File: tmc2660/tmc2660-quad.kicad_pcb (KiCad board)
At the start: 4 copper layers, 124 x 40 mm, 74 parts, among them J1 Power, J100 0R, J2 DataIn, J200 0R, J300 0R, J400 0R, M100 Mount, M101 Mount, M200 Mount, M201 Mount, M300 Mount, M301 Mount, M400 Mount, M401 Mount, P100 Motor, P200 Motor, P300 Motor, P400 Motor, U100 TMC2660, U200 TMC2660, U300 TMC2660, U400 TMC2660

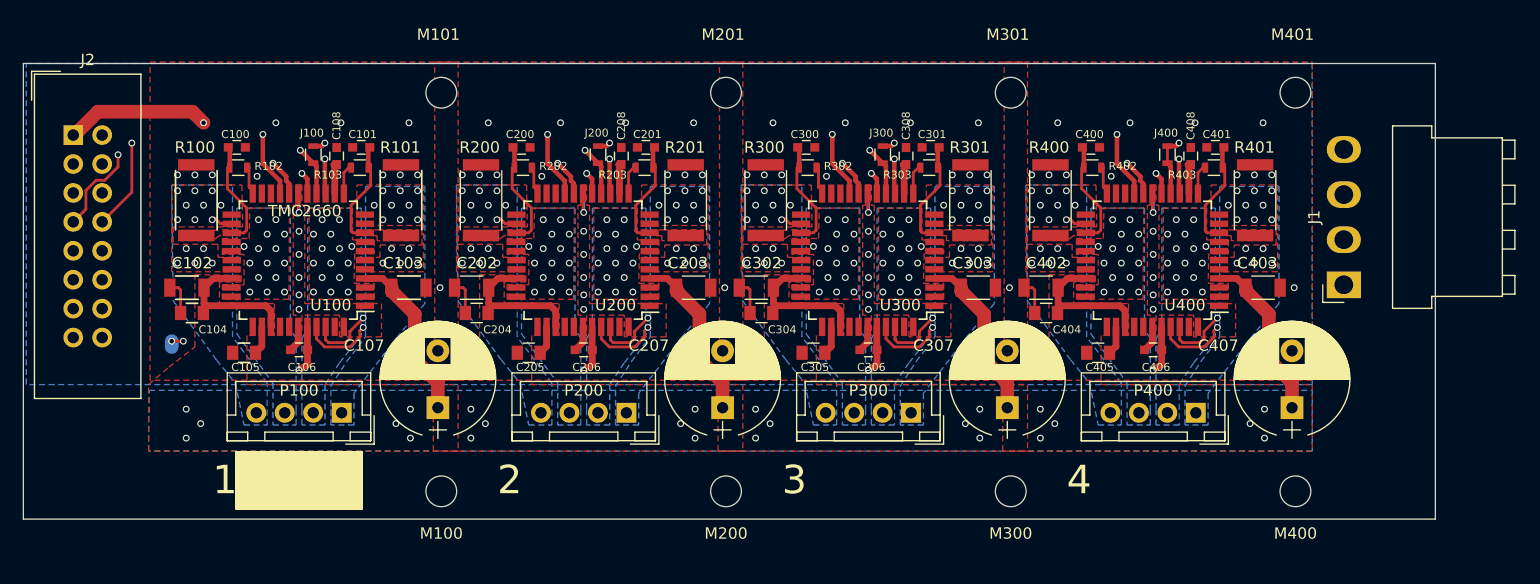
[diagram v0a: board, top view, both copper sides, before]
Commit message: Add leftmost screw holes; Move IDC connector down.
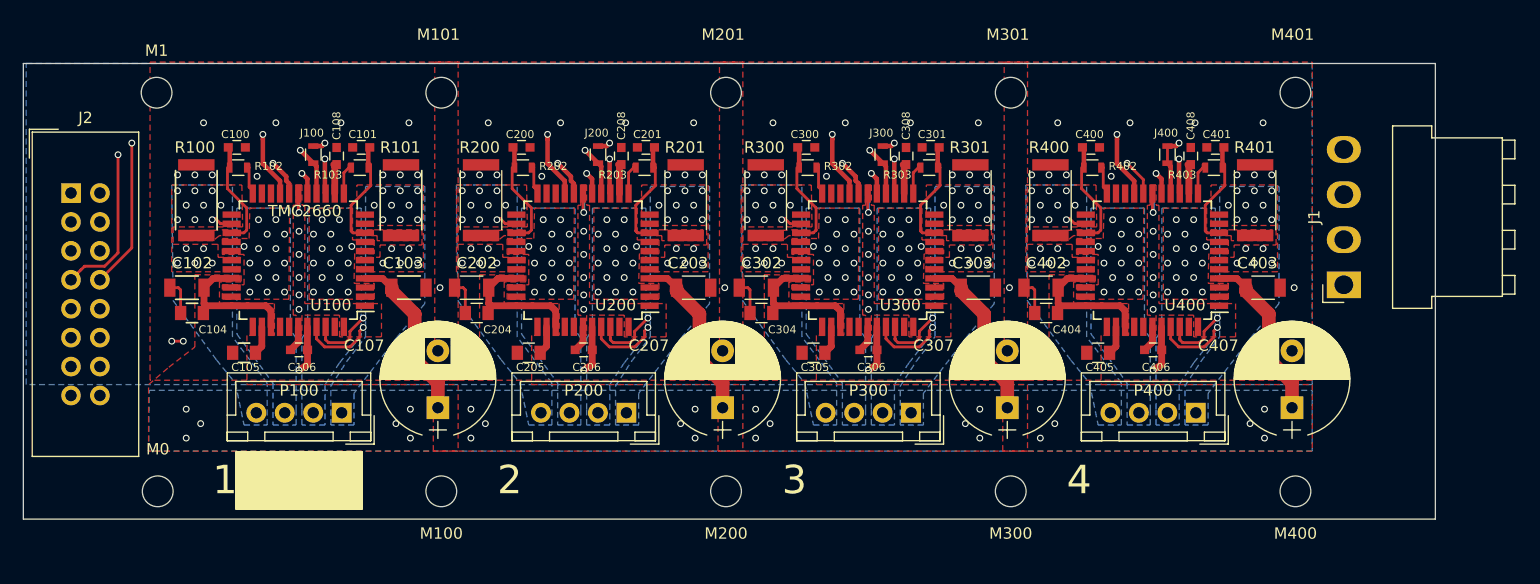
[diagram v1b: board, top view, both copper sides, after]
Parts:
- added M0: Mount, Mounting_Holes:MountingHole_2.7mm_M2.5, F.Cu at (71.4, 86.1)
- added M1: Mount, Mounting_Holes:MountingHole_2.7mm_M2.5, F.Cu at (71.3, 51.1)
- moved J2 5.09 mm to (63.8, 59.9)
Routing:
- net VCC: track 60.7 -> 38.4 mm
- net GND: track 52.5 -> 39.3 mm
- net GLOBAL_MISO: track 29.7 -> 35.4 mm
- net GLOBAL_MOSI: track 108.7 -> 113.9 mm
- net ~ENABLE: track 116.0 -> 120.1 mm
- net SCLK: track 103.1 -> 106.9 mm
- net STEP1: track 36.2 -> 32.7 mm
- net DIR4: track 108.9 -> 112.3 mm
- net CS: track 109.5 -> 112.8 mm
- net STEP4: track 110.8 -> 114.0 mm
- net DIR1: track 32.4 -> 30.7 mm
- net DIR3: track 83.6 -> 85.0 mm
- net STEP3: track 86.0 -> 87.0 mm
- net STEP2: track 60.8 -> 60.2 mm
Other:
- net class Default: clearance 0.127 -> 0.1524
- net class MotPower: clearance 0.127 -> 0.2032
- rule trace_clearance: 0.127 -> 0.1524

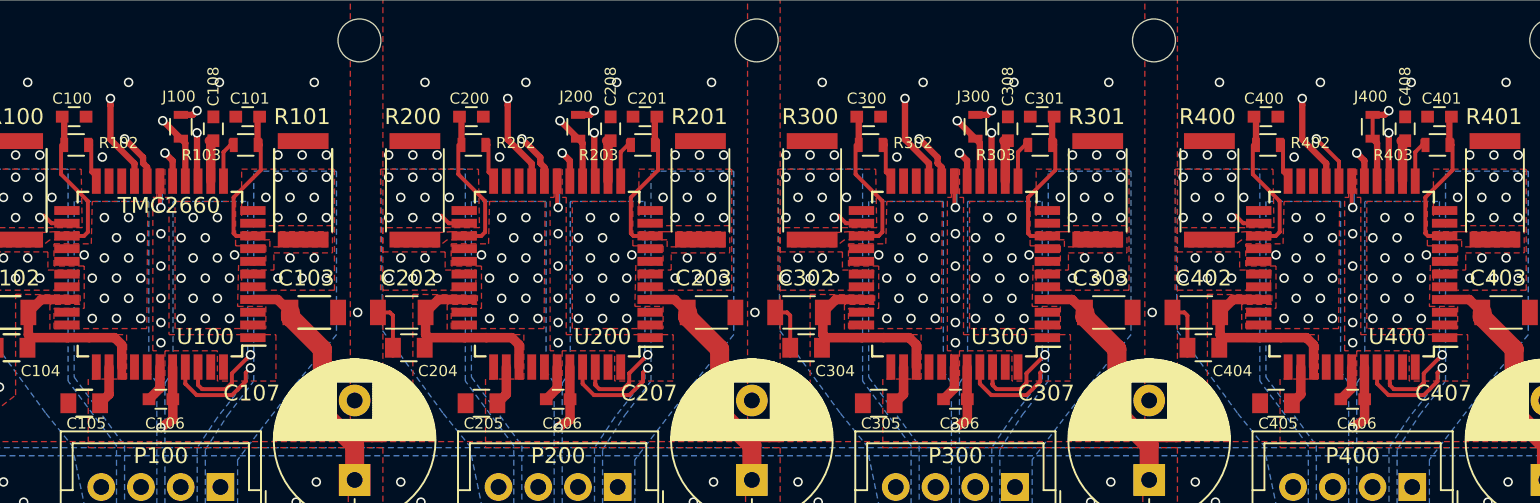
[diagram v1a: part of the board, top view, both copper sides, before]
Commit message: More conservative design rules in quad.
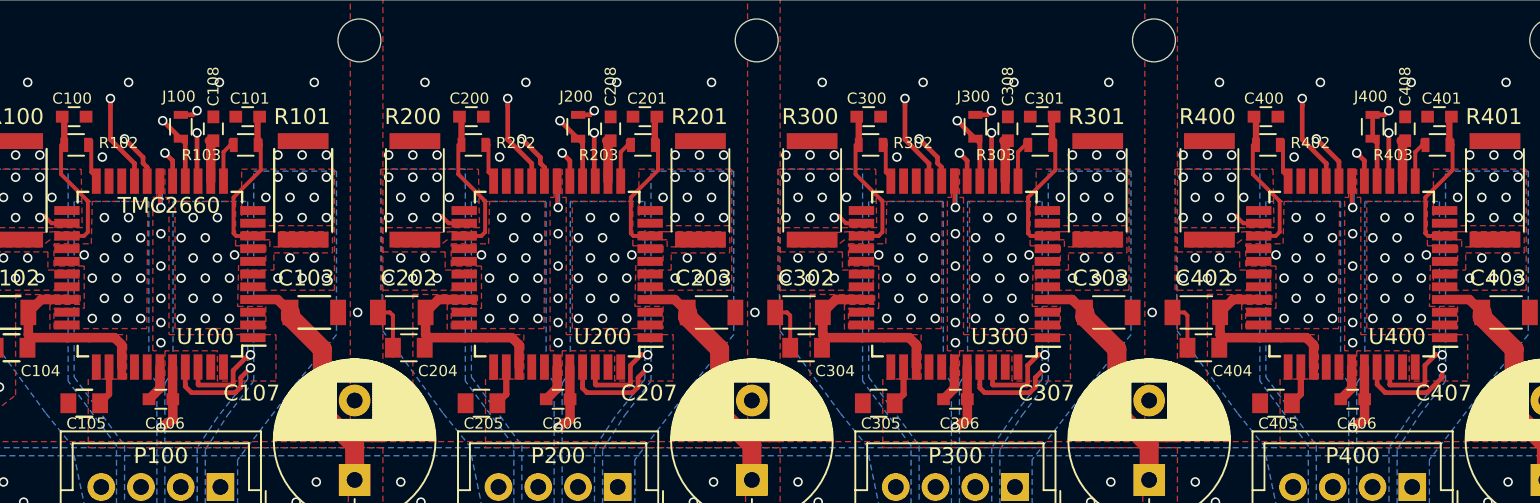
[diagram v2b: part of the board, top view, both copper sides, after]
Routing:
- net CS: track 112.8 -> 106.7 mm
- net GLOBAL_MISO: track 35.4 -> 32.1 mm
- net ~ENABLE: track 120.1 -> 117.0 mm
- net GLOBAL_MOSI: track 113.9 -> 111.4 mm
- net SCLK: track 106.9 -> 104.7 mm
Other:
- net class Default: clearance 0.1524 -> 0.18
- net class MotPower: clearance 0.2032 -> 0.21
- rule trace_clearance: 0.1524 -> 0.18

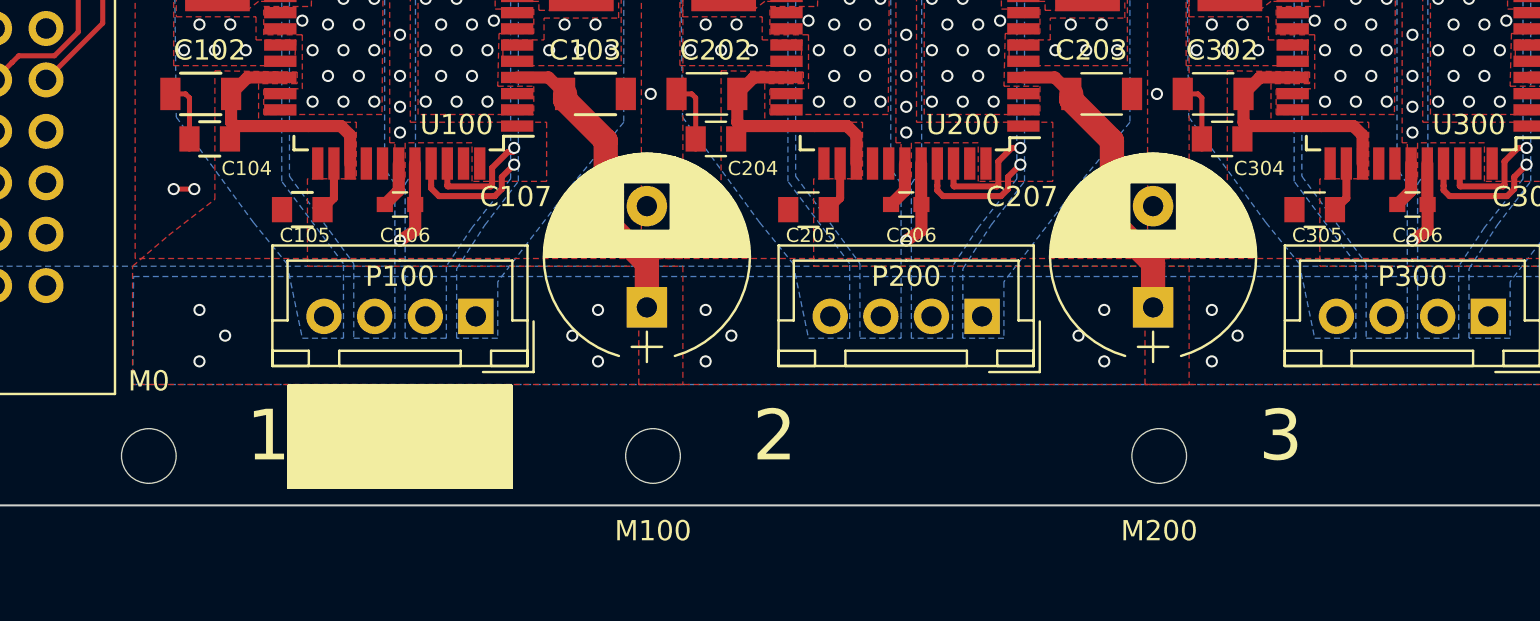
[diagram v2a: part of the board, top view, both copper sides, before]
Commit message: Routing of Step/Dir signals with new design rules.
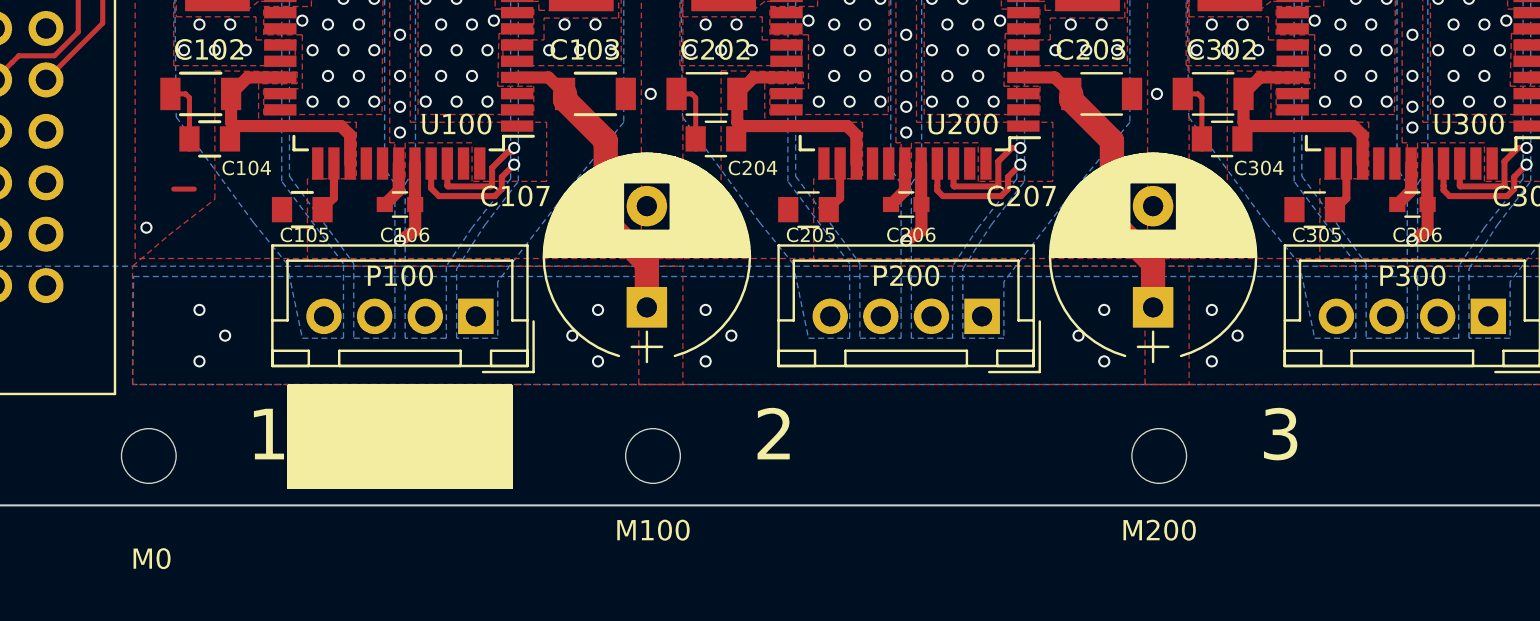
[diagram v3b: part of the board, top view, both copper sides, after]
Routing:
- net VCC: track 38.4 -> 54.1 mm
- net CS: track 106.7 -> 112.8 mm
- net GLOBAL_MISO: track 32.1 -> 35.4 mm
- net ~ENABLE: track 117.0 -> 120.1 mm
- net GLOBAL_MOSI: track 111.4 -> 113.9 mm
- net SCLK: track 104.7 -> 106.7 mm
- net DIR4: track 112.2 -> 111.5 mm
- net STEP4: track 114.1 -> 113.3 mm
- net STEP2: track 60.3 -> 60.8 mm
- net GND: vias 92 -> 91

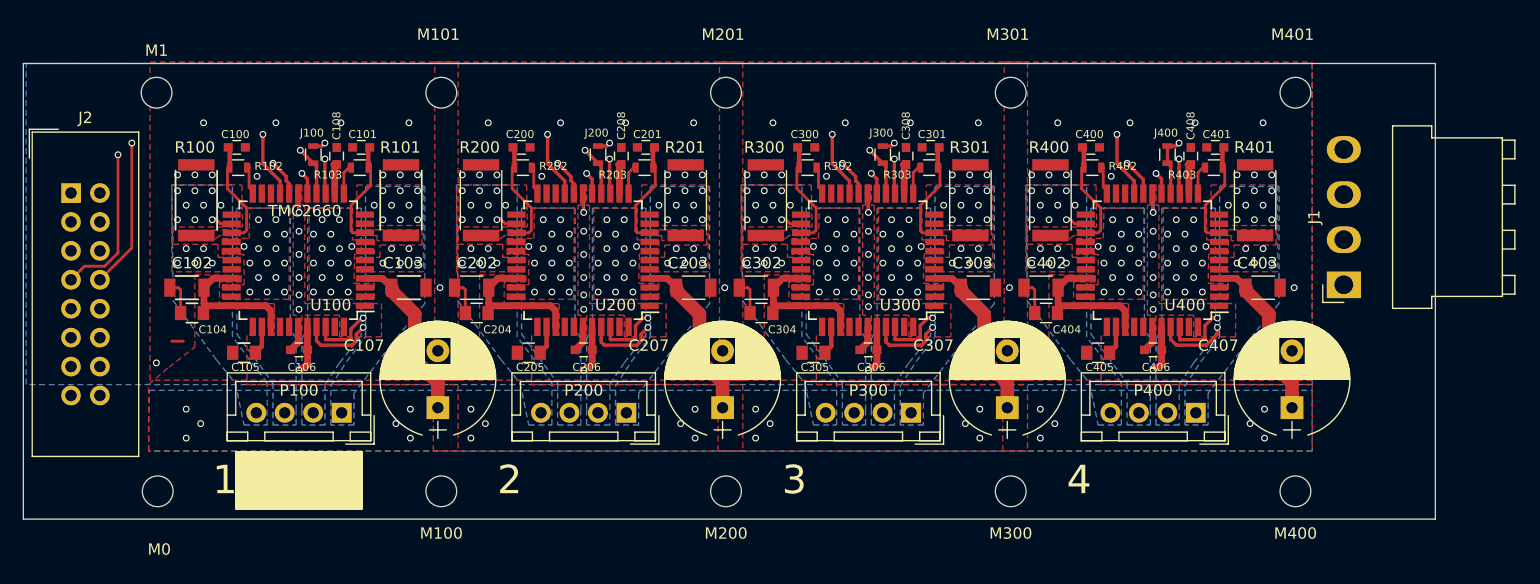
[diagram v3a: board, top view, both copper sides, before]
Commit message: Add a fuse.
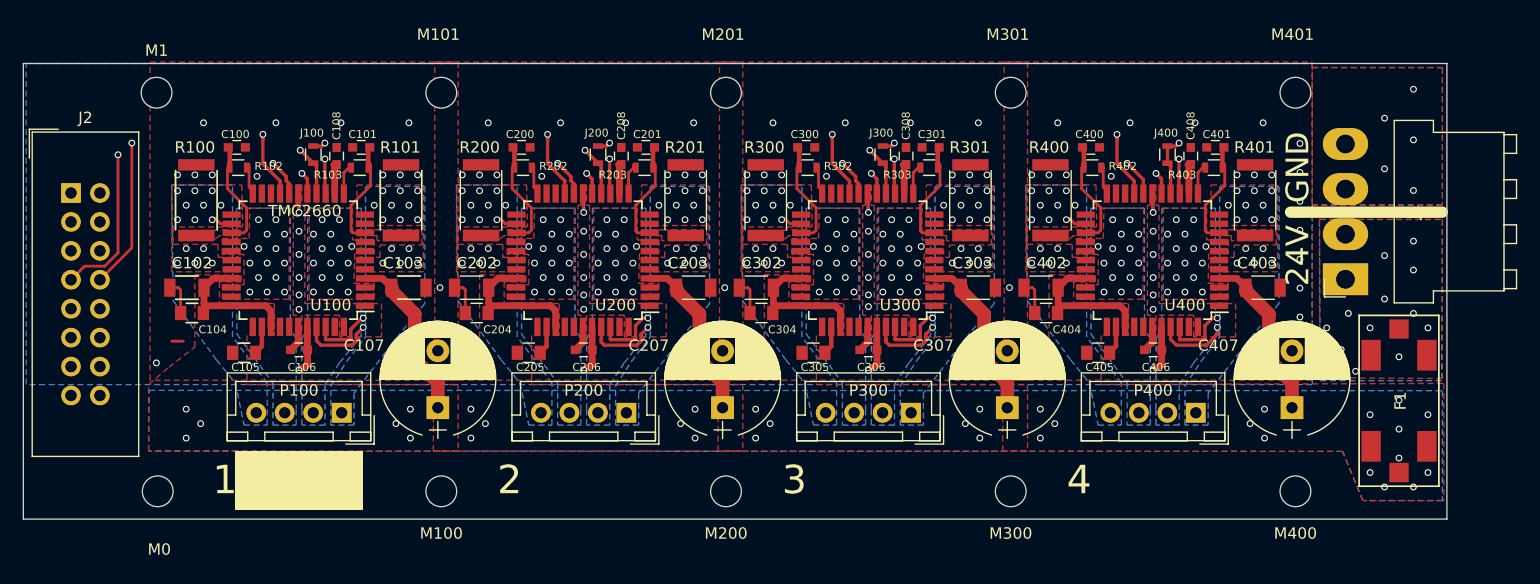
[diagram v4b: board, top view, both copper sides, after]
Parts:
- added F1: Fuse, Fuses:BladeFuse-Mini_Keystone-3586, F.Cu at (180.4, 78.1)
- moved J1 0.50 mm to (175.7, 67.5)
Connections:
- J1 pad 1: VMot -> /PowerIn
- J1 pad 2: VMot -> /PowerIn
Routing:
- net VMot: vias 24 -> 33
- net GND: vias 91 -> 102
- net /PowerIn: vias 0 -> 13
- added copper zone on B.Cu, net /PowerIn
- added copper zone on F.Cu, net /PowerIn
- added copper zone on In1.Cu, net /PowerIn
- added copper zone on In2.Cu, net /PowerIn
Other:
- board size 124 x 40 mm -> 125 x 40 mm
- board text added: "24V"
- board text added: "GND"

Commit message: Add labels.
o White label areas under connectors for the user to write
  the logical axis with sharpie.
o gitversion, github address etc.
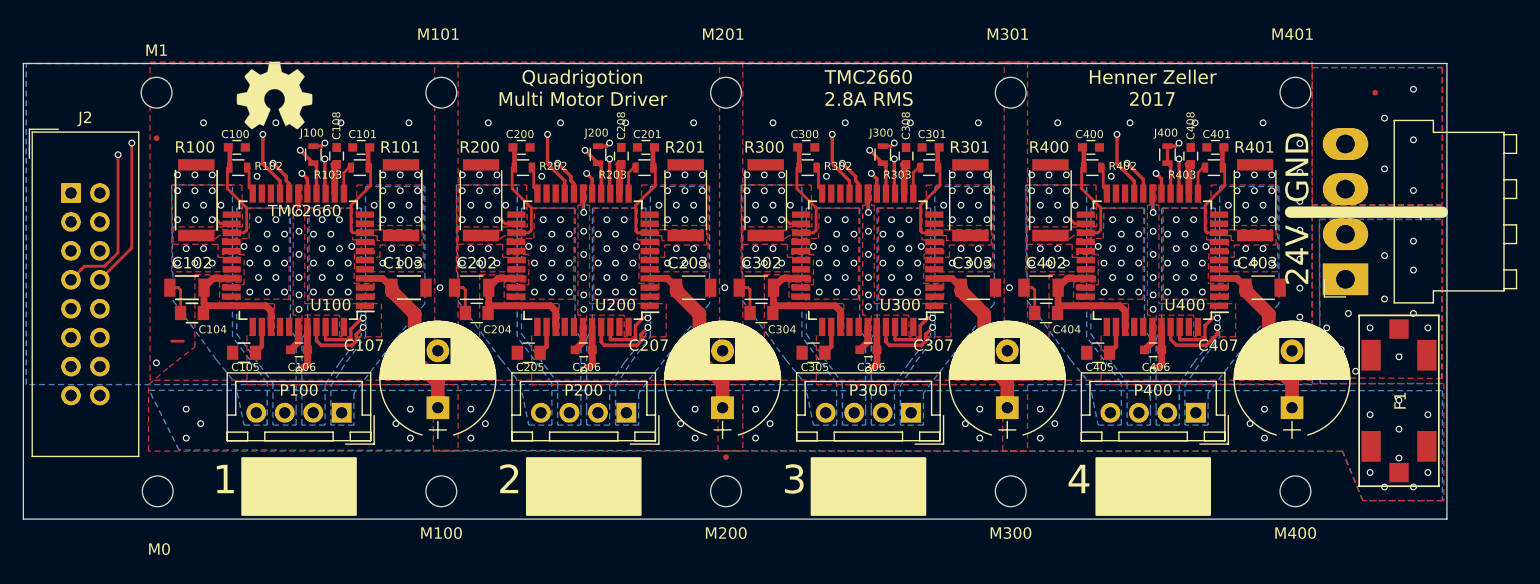
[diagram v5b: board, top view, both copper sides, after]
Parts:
- added REF**: Fiducial_0.5mm_Dia_1mm_Outer, Fiducials:Fiducial_0.5mm_Dia_1mm_Outer, F.Cu at (121.3, 83.1)
- added REF**: Fiducial_0.5mm_Dia_1mm_Outer, Fiducials:Fiducial_0.5mm_Dia_1mm_Outer, F.Cu at (178.3, 51.1)
- added REF**: Fiducial_0.5mm_Dia_1mm_Outer, Fiducials:Fiducial_0.5mm_Dia_1mm_Outer, F.Cu at (71.3, 55.1)
- added REF***: OSHW-Symbol_6.7x6mm_SilkScreen, Symbols:OSHW-Symbol_6.7x6mm_SilkScreen, F.Cu at (81.7, 51.3)
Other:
- board text added: "%%gitversion%%"
- board text added: "H"
- board text added: "Henner Zeller 2017"
- board text added: "Quadrigotion Multi Motor Driver"
- board text added: "TMC2660 2.8A RMS"
- board text added: "Z"
- board text added: "github.com/hzeller/quadrigotion"
